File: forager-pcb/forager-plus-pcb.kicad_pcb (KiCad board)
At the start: 2 copper layers, 114.6 x 96.3 mm, 25 parts, among them U1 XIAO nRF52840 Plus

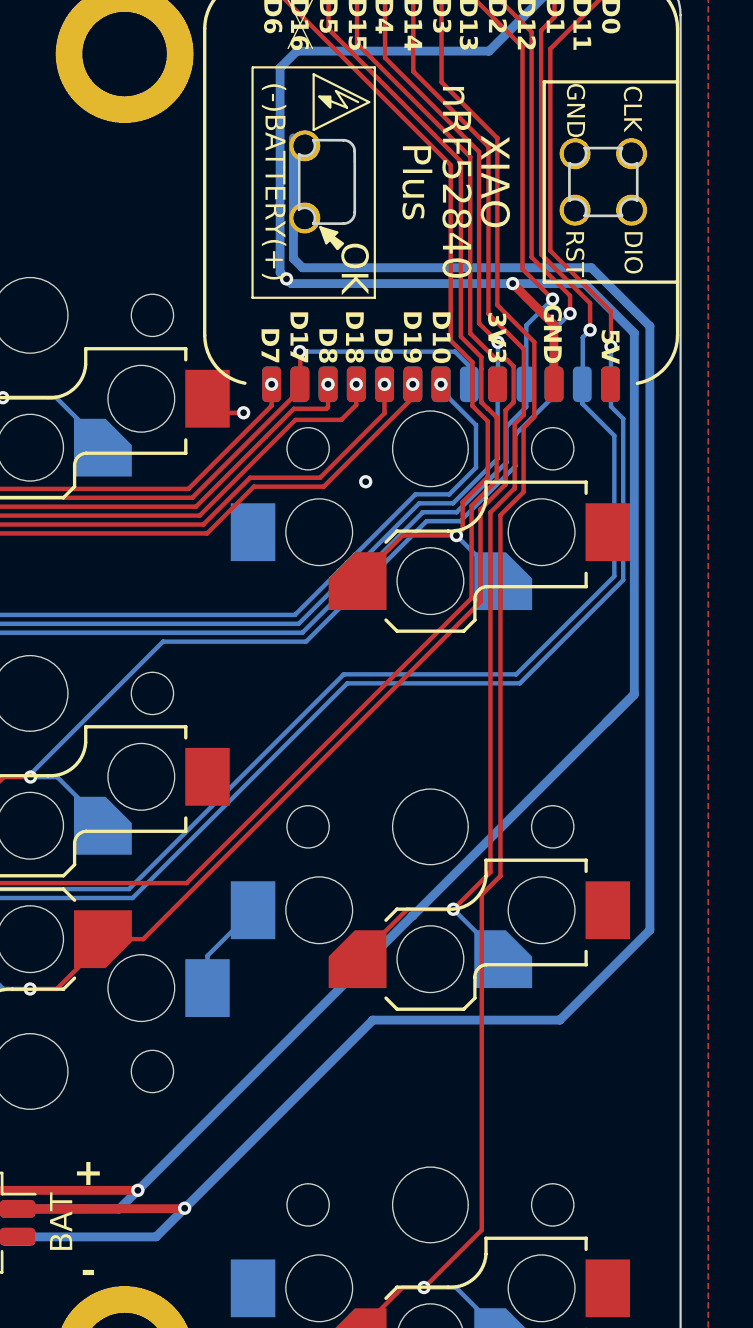
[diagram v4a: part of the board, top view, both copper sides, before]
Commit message: Add MSK12C02 power switch - LCSC C431540 or similar, SMD
These should both be up off (towards controller corner), and
down on (away from controller). Ought to be able to solder
bridge the pads if not using the switch?

Hat tip https://github.com/letmegobacktosleep/forager/tree/power-switch/forager-pcb
Using same location, so same case modifications should work.
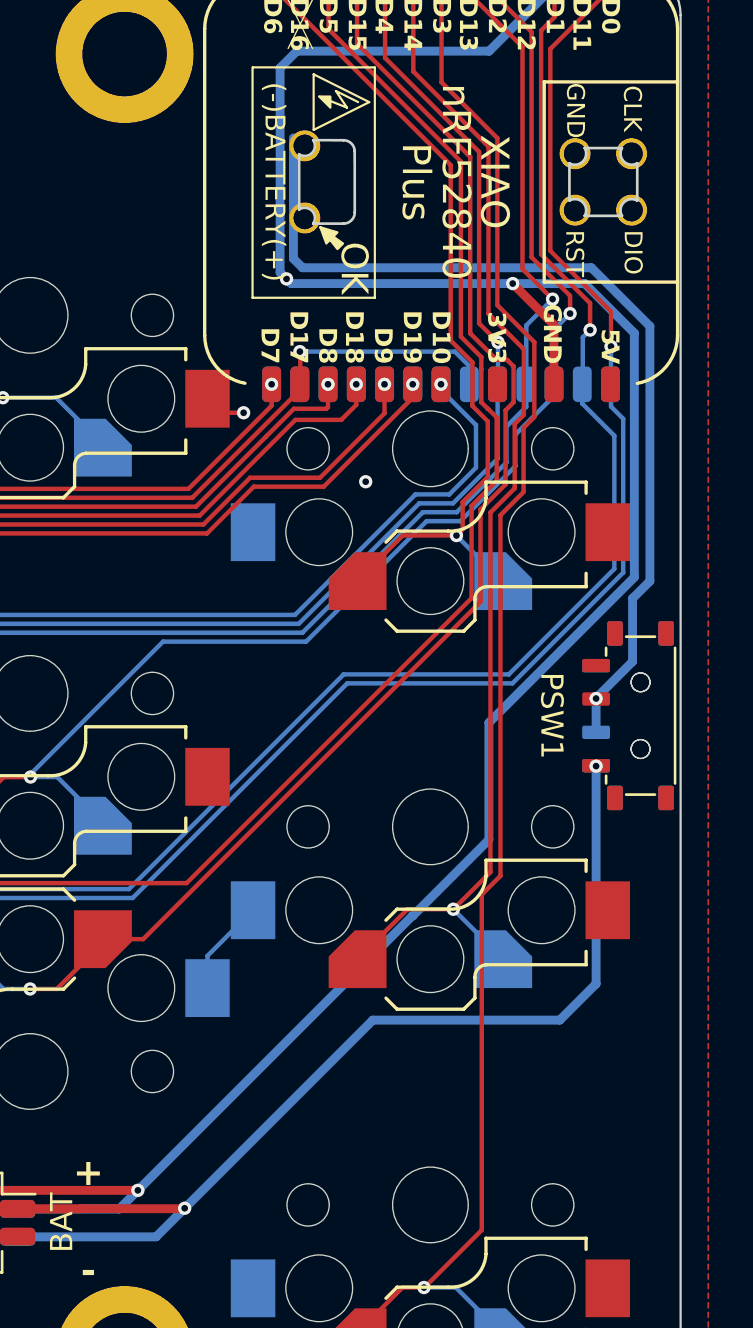
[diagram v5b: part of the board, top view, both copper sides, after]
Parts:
- added PSW1: SW_SPDT, PCM_marbastlib-various:SW_MSK12C02-HB, F.Cu at (116.5, -16.0)
- added PSW2: SW_SPDT, PCM_marbastlib-various:SW_MSK12C02-HB, B.Cu at (116.5, -16.0)
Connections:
- BAT pad 1: BAT -> BAT_CON (x2)
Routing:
- net BAT: track 92.7 -> 42.0 mm
- net BAT_CON: track 0.00 -> 49.2 mm, vias 0 -> 2
- net GND: track 118.4 -> 116.6 mm

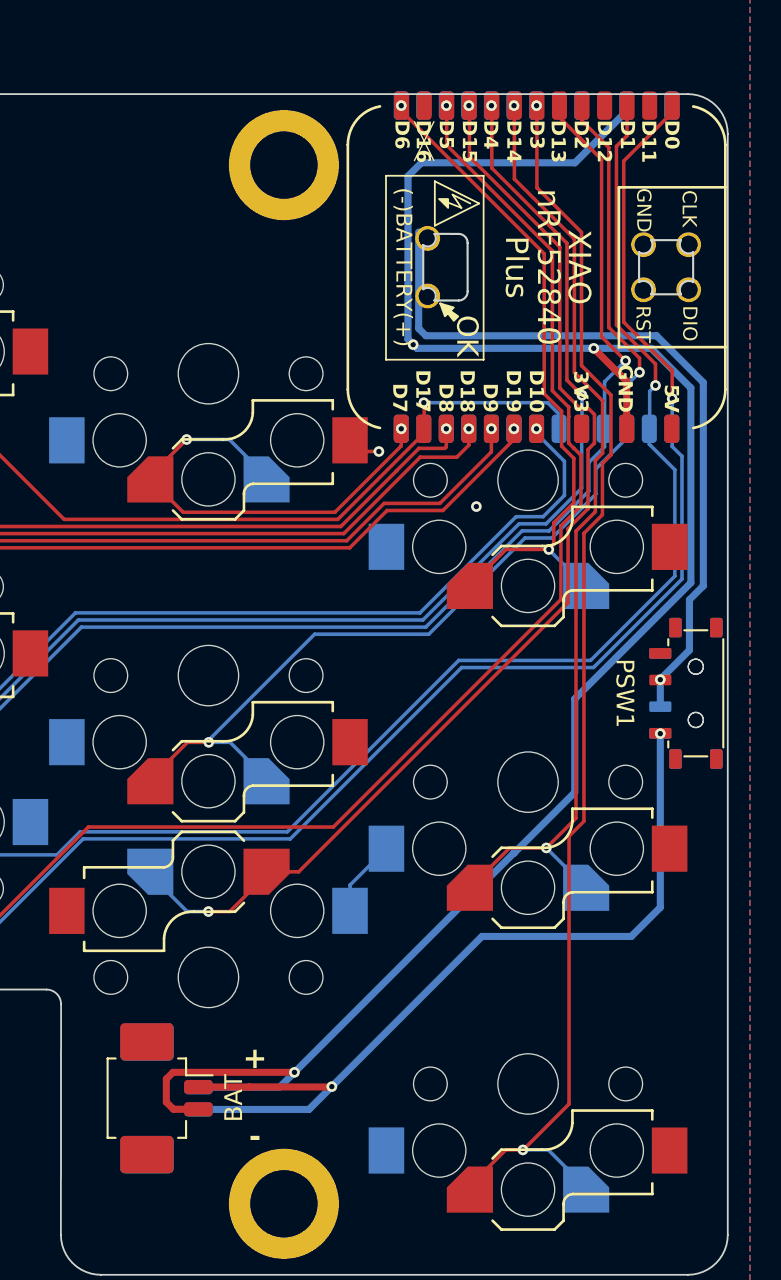
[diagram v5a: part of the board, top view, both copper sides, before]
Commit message: Move battery connector back (for plug); thru-hole solder points,
I rotated the battery connection and moved back to give more clearance
for the plug - beware the bottom case rib.

Hat tip https://github.com/letmegobacktosleep/forager/tree/power-switch/forager-pcb
for the thru-hole solder point idea, which seems a little easier to use.
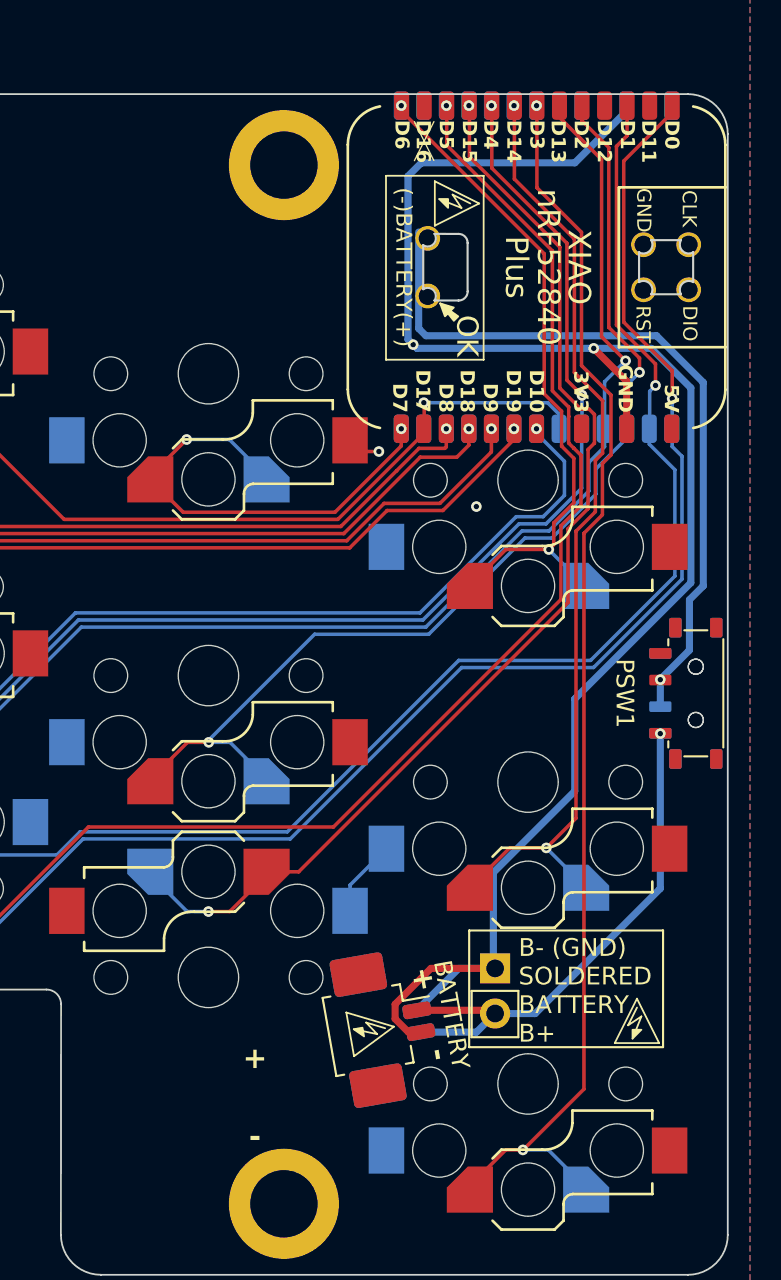
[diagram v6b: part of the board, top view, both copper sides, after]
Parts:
- removed the BAT at (86.0, 6.80)
- removed the BAT at (86.0, 6.81)
- added ?: , clipboard:c6e4976e-07e6-4aae-98ea-2f932d7c0aa1, F.Cu at (111.9, 3.70)
- added ?: , clipboard:c6e4976e-07e6-4aae-98ea-2f932d7c0aa1, F.Cu at (96.8, 1.98)
- added ?: , clipboard:c6e4976e-07e6-4aae-98ea-2f932d7c0aa1, B.Cu at (114.4, 3.71)
- added ?: , clipboard:c6e4976e-07e6-4aae-98ea-2f932d7c0aa1, B.Cu at (97.2, 4.44)
- added BAT: Molex_PicoBlade_53261-0271_1x02-1MP_P1.25mm_Horizontal, Connector_Molex:Molex_PicoBlade_53261-0271_1x02-1MP_P1.25mm_Horizontal, B.Cu at (98.5, 2.88)
- added BATTERY: Molex_PicoBlade_53261-0271_1x02-1MP_P1.25mm_Horizontal, Connector_Molex:Molex_PicoBlade_53261-0271_1x02-1MP_P1.25mm_Horizontal, F.Cu at (98.5, 2.88)
- added J4: Conn_01x02_Pin, Connector_PinHeader_2.54mm:PinHeader_1x02_P2.54mm_Vertical, B.Cu at (105.1, -0.51)
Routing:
- net BAT_CON: track 49.2 -> 29.8 mm, vias 2 -> 1
- net GND: track 116.6 -> 104.0 mm, vias 6 -> 5
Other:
- board text added: "(GND) B- SOLDERED BATTERY B+"
- board text added: "B- (GND) SOLDERED BATTERY B+"
- board text added: "BATTERY"
